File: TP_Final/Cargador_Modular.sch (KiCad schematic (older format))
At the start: 0 parts

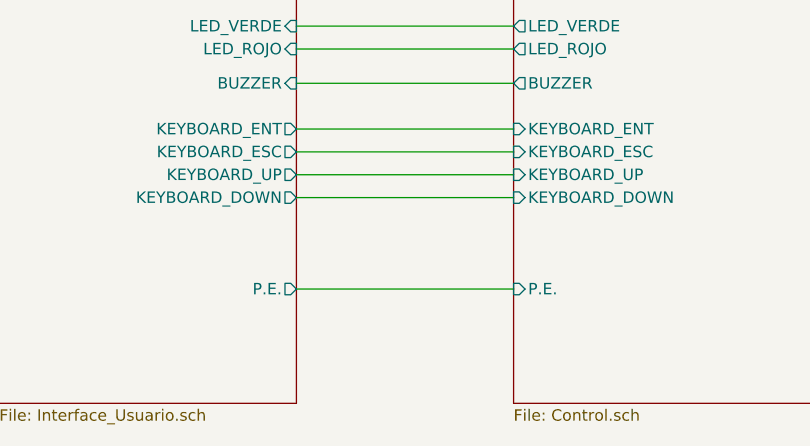
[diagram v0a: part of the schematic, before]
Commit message: Se completa rotulo
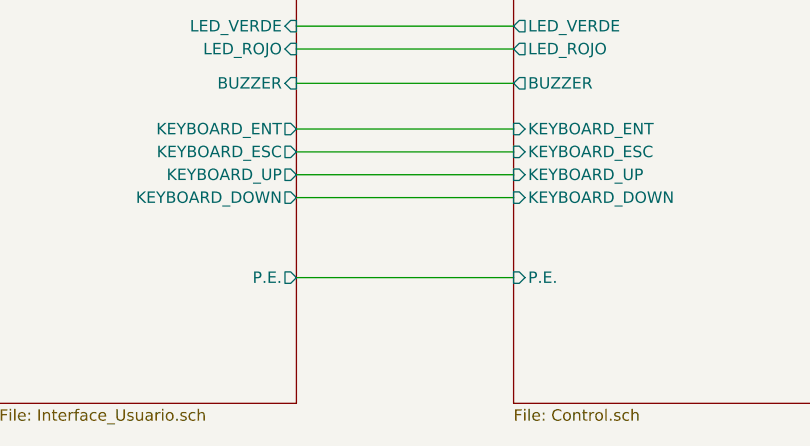
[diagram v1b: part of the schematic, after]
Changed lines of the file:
@@
 Sheet 1 4
 Title "Cargador modular de baterias industriales"
-Date "2021-03-18"
-Rev "0"
+Date "2021-03-26"
+Rev "1"
 Comp "proba"
-Comment1 "Revisor: Diego Brengi"
-Comment2 "Autor: Felipe A. Calcavecchia"
-Comment3 ""
-Comment4 ""
+Comment1 "Creative Commons Attribution-NonCommercial-ShareAlike 4.0 International License"
+Comment2 "Revisor 2: Cristian A. Trinidad"
+Comment3 "Revisor 1: Diego Brengi"
+Comment4 "Autor: Felipe A. Calcavecchia"
 $EndDescr
 $Sheet
@@
 F29 "LED_ROJO" O L 4200 3700 50
 F30 "BUZZER" O L 4200 3850 50
-F31 "P.E." I L 4200 4750 50
+F31 "P.E." I L 4200 4700 50
 $EndSheet
 Wire Wire Line
@@
 	5500 3050 6450 3050
 Wire Wire Line
-	3250 4750 4200 4750
+	3250 4700 4200 4700
 $Sheet
 S 1950 1950 1300 3300
@@
 F20 "KEYBOARD_UP" O R 3250 4250 50
 F21 "KEYBOARD_DOWN" O R 3250 4350 50
-F22 "P.E." O R 3250 4750 50
+F22 "P.E." O R 3250 4700 50
 $EndSheet
 Text Notes 2900 1100 0    118  Italic 24

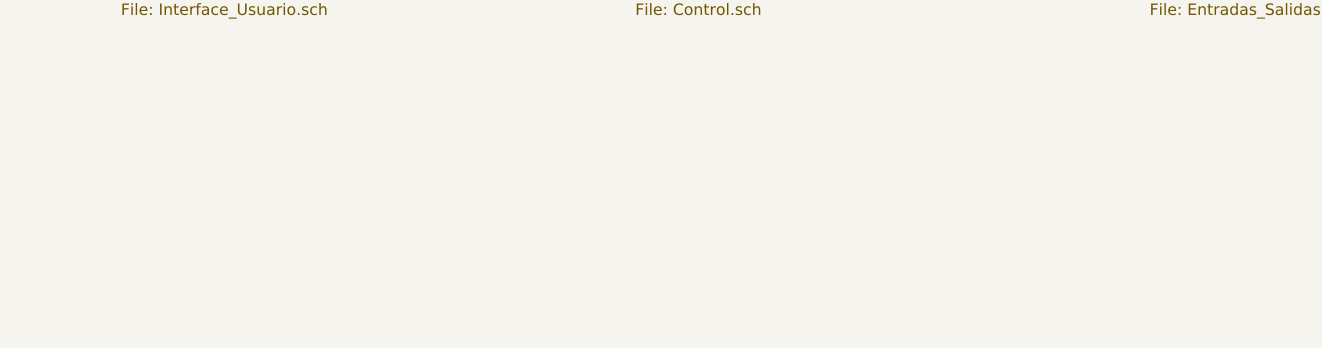
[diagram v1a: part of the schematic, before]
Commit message: Agrego agujeros de montaje y fiduciales al esquematico
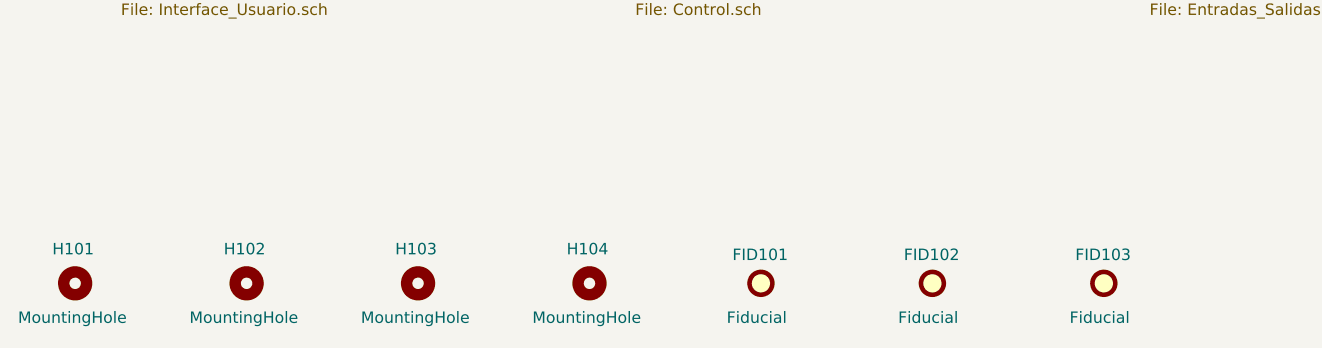
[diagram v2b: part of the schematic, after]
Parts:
- added FID101, FID102, FID103: Fiducial, Fiducial:Fiducial_0.75mm_Mask1.5mm, symbol Mechanical:Fiducial
- added H101, H102, H103, H104: MountingHole, MountingHole:MountingHole_4.5mm_Pad, symbol Mechanical:MountingHole
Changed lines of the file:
@@
 EndData
 $EndBitmap
+$Comp
+L Mechanical:MountingHole H101
+U 1 1 608D0512
+P 1750 6500
+F 0 "H101" H 1650 6650 50  0000 L CNN
+F 1 "MountingHole" H 1500 6350 50  0000 L CNN
+F 2 "MountingHole:MountingHole_4.5mm_Pad" H 1750 6500 50  0001 C CNN
+F 3 "~" H 1750 6500 50  0001 C CNN
+	1    1750 6500
+	1    0    0    -1
+$EndComp
+$Comp
+L Mechanical:MountingHole H102
+U 1 1 608D1797
+P 2500 6500
+F 0 "H102" H 2400 6650 50  0000 L CNN
+F 1 "MountingHole" H 2250 6350 50  0000 L CNN
+F 2 "MountingHole:MountingHole_4.5mm_Pad" H 2500 6500 50  0001 C CNN
+F 3 "~" H 2500 6500 50  0001 C CNN
+	1    2500 6500
+	1    0    0    -1
+$EndComp
+$Comp
+L Mechanical:MountingHole H103
+U 1 1 608D1907
+P 3250 6500
+F 0 "H103" H 3150 6650 50  0000 L CNN
+F 1 "MountingHole" H 3000 6350 50  0000 L CNN
+F 2 "MountingHole:MountingHole_4.5mm_Pad" H 3250 6500 50  0001 C CNN
+F 3 "~" H 3250 6500 50  0001 C CNN
+	1    3250 6500
+	1    0    0    -1
+$EndComp
+$Comp
+L Mechanical:MountingHole H104
+U 1 1 608D1A12
+P 4000 6500
+F 0 "H104" H 3900 6650 50  0000 L CNN
+F 1 "MountingHole" H 3750 6350 50  0000 L CNN
+F 2 "MountingHole:MountingHole_4.5mm_Pad" H 4000 6500 50  0001 C CNN
+F 3 "~" H 4000 6500 50  0001 C CNN
+	1    4000 6500
+	1    0    0    -1
+$EndComp
+$Comp
+L Mechanical:Fiducial FID101
+U 1 1 60720655
+P 4750 6500
+F 0 "FID101" H 4625 6625 50  0000 L CNN
+F 1 "Fiducial" H 4600 6350 50  0000 L CNN
+F 2 "Fiducial:Fiducial_0.75mm_Mask1.5mm" H 4750 6500 50  0001 C CNN
+F 3 "~" H 4750 6500 50  0001 C CNN
+	1    4750 6500
+	1    0    0    -1
+$EndComp
+$Comp
+L Mechanical:Fiducial FID102
+U 1 1 60720A17
+P 5500 6500
+F 0 "FID102" H 5375 6625 50  0000 L CNN
+F 1 "Fiducial" H 5350 6350 50  0000 L CNN
+F 2 "Fiducial:Fiducial_0.75mm_Mask1.5mm" H 5500 6500 50  0001 C CNN
+F 3 "~" H 5500 6500 50  0001 C CNN
+	1    5500 6500
+	1    0    0    -1
+$EndComp
+$Comp
+L Mechanical:Fiducial FID103
+U 1 1 60720B5E
+P 6250 6500
+F 0 "FID103" H 6125 6625 50  0000 L CNN
+F 1 "Fiducial" H 6100 6350 50  0000 L CNN
+F 2 "Fiducial:Fiducial_0.75mm_Mask1.5mm" H 6250 6500 50  0001 C CNN
+F 3 "~" H 6250 6500 50  0001 C CNN
+	1    6250 6500
+	1    0    0    -1
+$EndComp
 $EndSCHEMATC

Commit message: Se finaliza el diseño del PCB
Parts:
- added FID104, FID105, FID106: Fiducial, Fiducial:Fiducial_0.75mm_Mask1.5mm, symbol Mechanical:Fiducial
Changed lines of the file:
@@
+	1    0    0    -1
+$EndComp
+$Comp
+L Mechanical:Fiducial FID104
+U 1 1 607CA507
+P 4750 7100
+F 0 "FID104" H 4625 7225 50  0000 L CNN
+F 1 "Fiducial" H 4600 6950 50  0000 L CNN
+F 2 "Fiducial:Fiducial_0.75mm_Mask1.5mm" H 4750 7100 50  0001 C CNN
+F 3 "~" H 4750 7100 50  0001 C CNN
+	1    4750 7100
+	1    0    0    -1
+$EndComp
+$Comp
+L Mechanical:Fiducial FID105
+U 1 1 607CA50D
+P 5500 7100
+F 0 "FID105" H 5375 7225 50  0000 L CNN
+F 1 "Fiducial" H 5350 6950 50  0000 L CNN
+F 2 "Fiducial:Fiducial_0.75mm_Mask1.5mm" H 5500 7100 50  0001 C CNN
+F 3 "~" H 5500 7100 50  0001 C CNN
+	1    5500 7100
+	1    0    0    -1
+$EndComp
+$Comp
+L Mechanical:Fiducial FID106
+U 1 1 607CA513
+P 6250 7100
+F 0 "FID106" H 6125 7225 50  0000 L CNN
+F 1 "Fiducial" H 6100 6950 50  0000 L CNN
+F 2 "Fiducial:Fiducial_0.75mm_Mask1.5mm" H 6250 7100 50  0001 C CNN
+F 3 "~" H 6250 7100 50  0001 C CNN
+	1    6250 7100
 	1    0    0    -1
 $EndComp
